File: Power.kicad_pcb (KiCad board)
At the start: 6 copper layers, 53 x 108.8 mm, 293 parts, among them Y1 16M

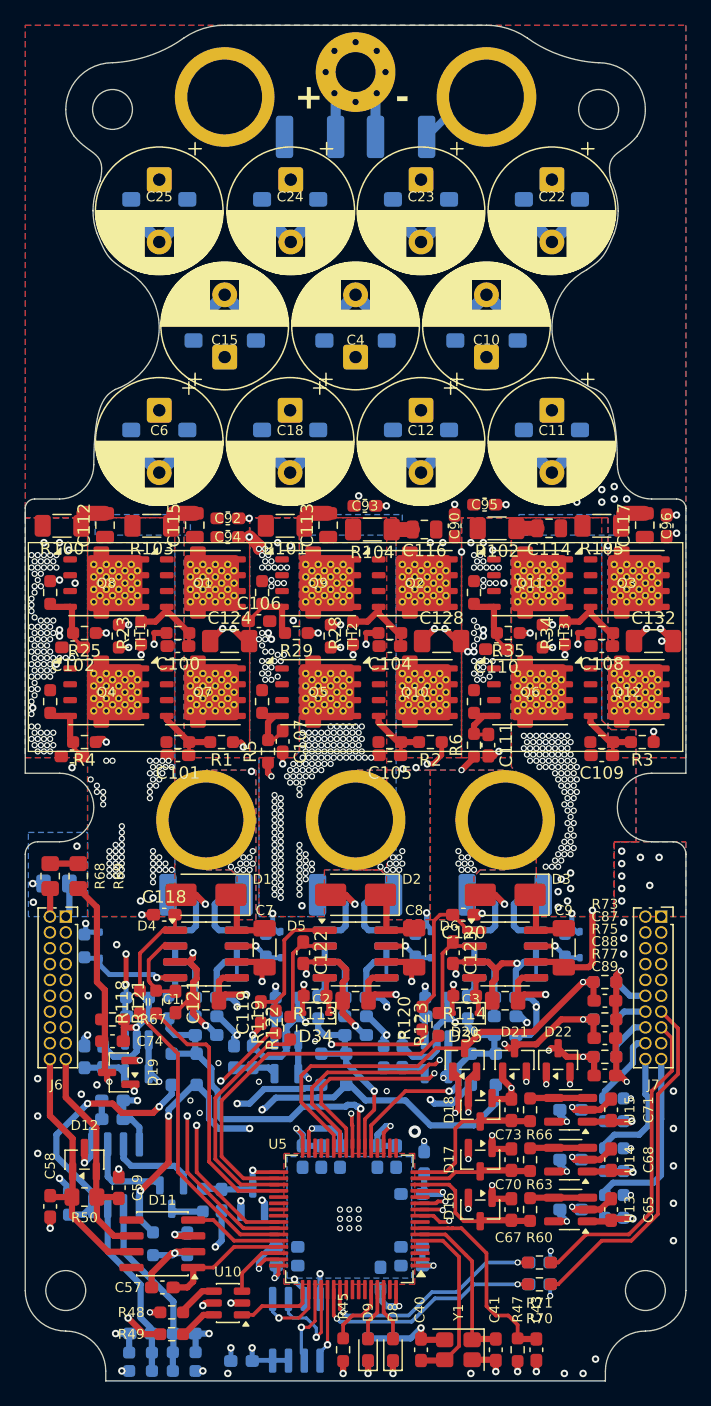
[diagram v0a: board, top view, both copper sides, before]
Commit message: rev0.1-shift3, шаг 16 (lay_S3d.py): пары HO/SW фаз C и B на In4 с зазором 0.25 мм вместо 0.5; одна ширина на цепь по всем слоям (46 цепей, силовые не трогал)
- HO сдвинута к SW, углы концентричные; площадь петли затвора HS на этих участках −31 % (C) / −21 % (B)
- 0.5: LO, затворы R_g → G (C100–C111), D8/D9-K; 0.3: HO/SW, термисторы, сигналы МК; где 0.5 не проходит у выводов МК — 0.3 целиком
- DRC 0/0/0, track_scan 0, hv.py 23 (было 24); shift3.sh с 515455d даёт ту же плату

Co-Authored-By: Claude Opus 5.5 <noreply@anthropic.com>
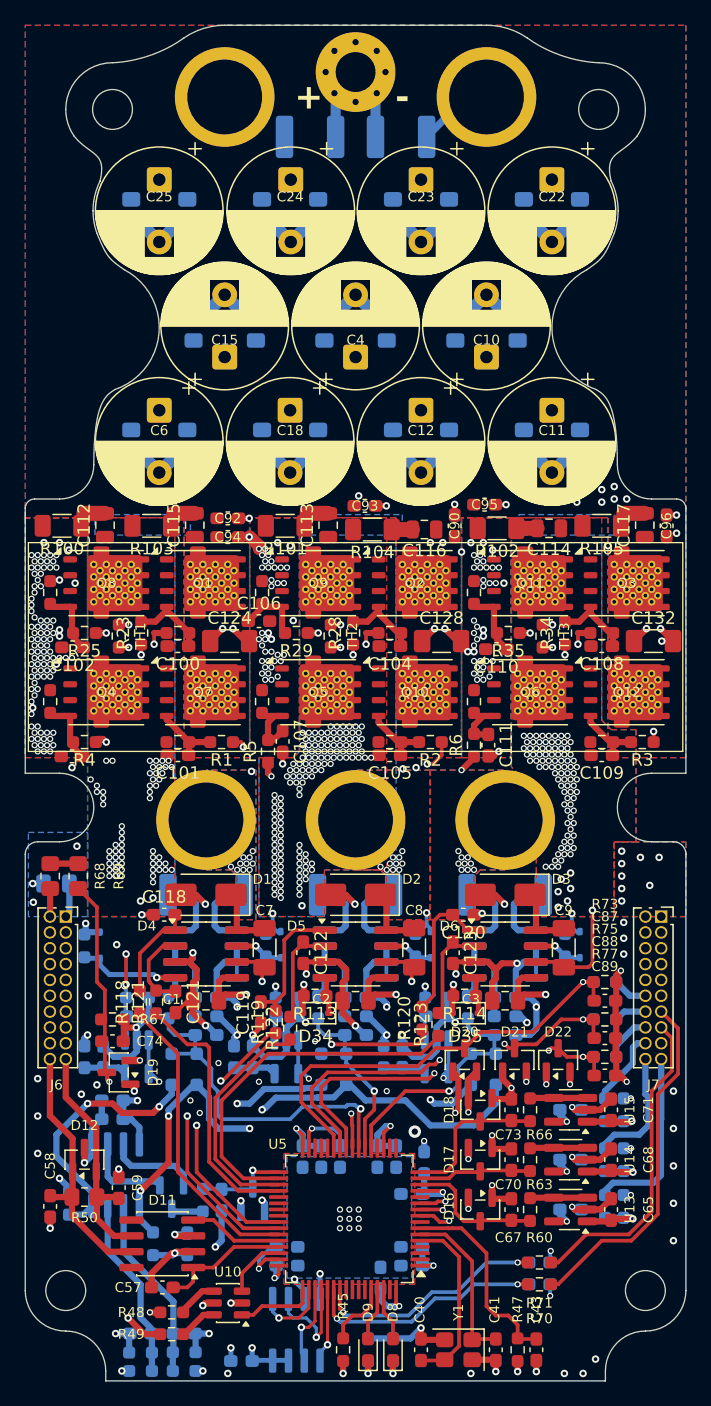
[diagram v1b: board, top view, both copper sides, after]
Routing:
- net /Driver_2/HO: track 31.5 -> 31.0 mm

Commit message: Переразводка владельца в зоне МК: SWD, Temp_PCB_1/2, VDC_MCU с In4 на In2; .gitignore: tmp/; CHANGELOG: опора B.Cu под INA и оценка обмена In3/In4
- ниже y 112 на In4 только GND; под дорожками B.Cu (y > 100) земля на 325 мм из 425 (было 300); DRC 0/0/0, новые отрезки 0/45/90°
- оставшиеся провалы: магистраль +12V и стояки к D1–D3 на In4 под INA240; обмен In3/In4 переносит дыры на In2 (аналог In2 без земли 9.5 → 36 мм)
- проба (+12V на In2, стояки D2/D3 на In1): аналог B.Cu без земли 61 → 38 мм, остаток — антипады своих виа и Kelvin-линии над фазной медью
- tmp/ — временные файлы работы, вне git

Co-Authored-By: Claude Opus 5.5 <noreply@anthropic.com>
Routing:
- net /VDC_MCU: track 44.2 -> 48.5 mm
- net Net-(D24-A): track 59.2 -> 61.3 mm
- net /Temp_PCB_1_MCU: track 21.4 -> 19.7 mm
- net /Temp_PCB_2_MCU: track 27.1 -> 25.6 mm
- net GND: track 252.0 -> 253.3 mm, vias 277 -> 276
- net +3.3V: track 143.8 -> 145.1 mm
- net /SWDIO_IN: track 28.3 -> 29.4 mm, vias 2 -> 1
- net /Temp_PCB_3_MCU: track 43.3 -> 42.4 mm
- net /SWCLK_IN: track 29.7 -> 30.5 mm, vias 2 -> 1
